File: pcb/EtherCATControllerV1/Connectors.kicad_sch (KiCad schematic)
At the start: 16 parts, among them J1 Conn_01x04, J2 Conn_01x05_Socket, J3 Conn_01x04_Socket, T1 H1102NLT

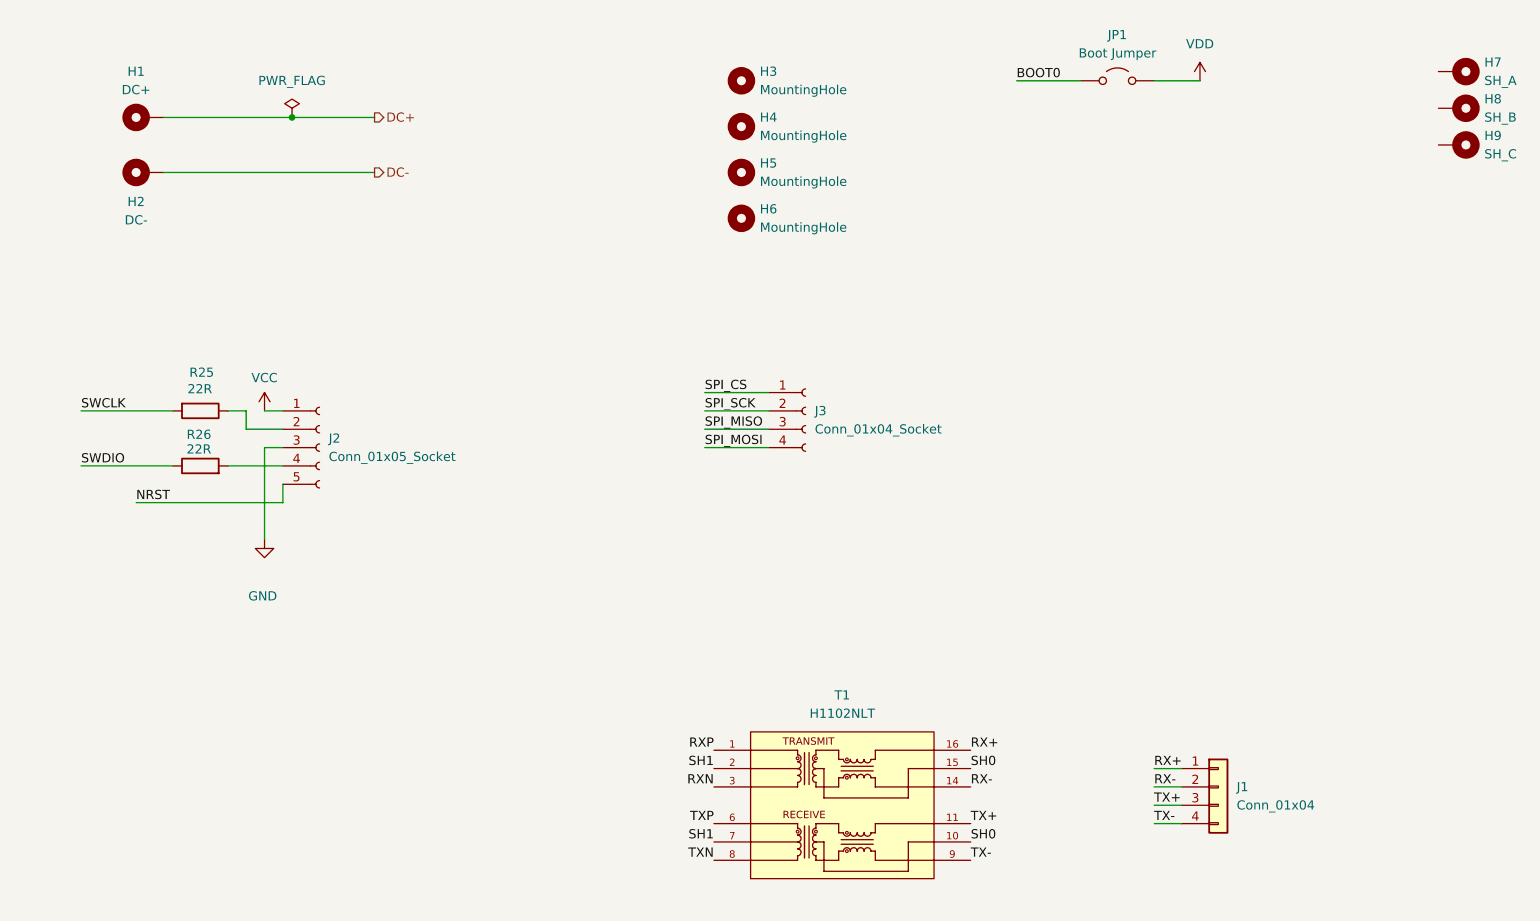
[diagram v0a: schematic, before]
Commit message: Initial design without Ethernet connectors
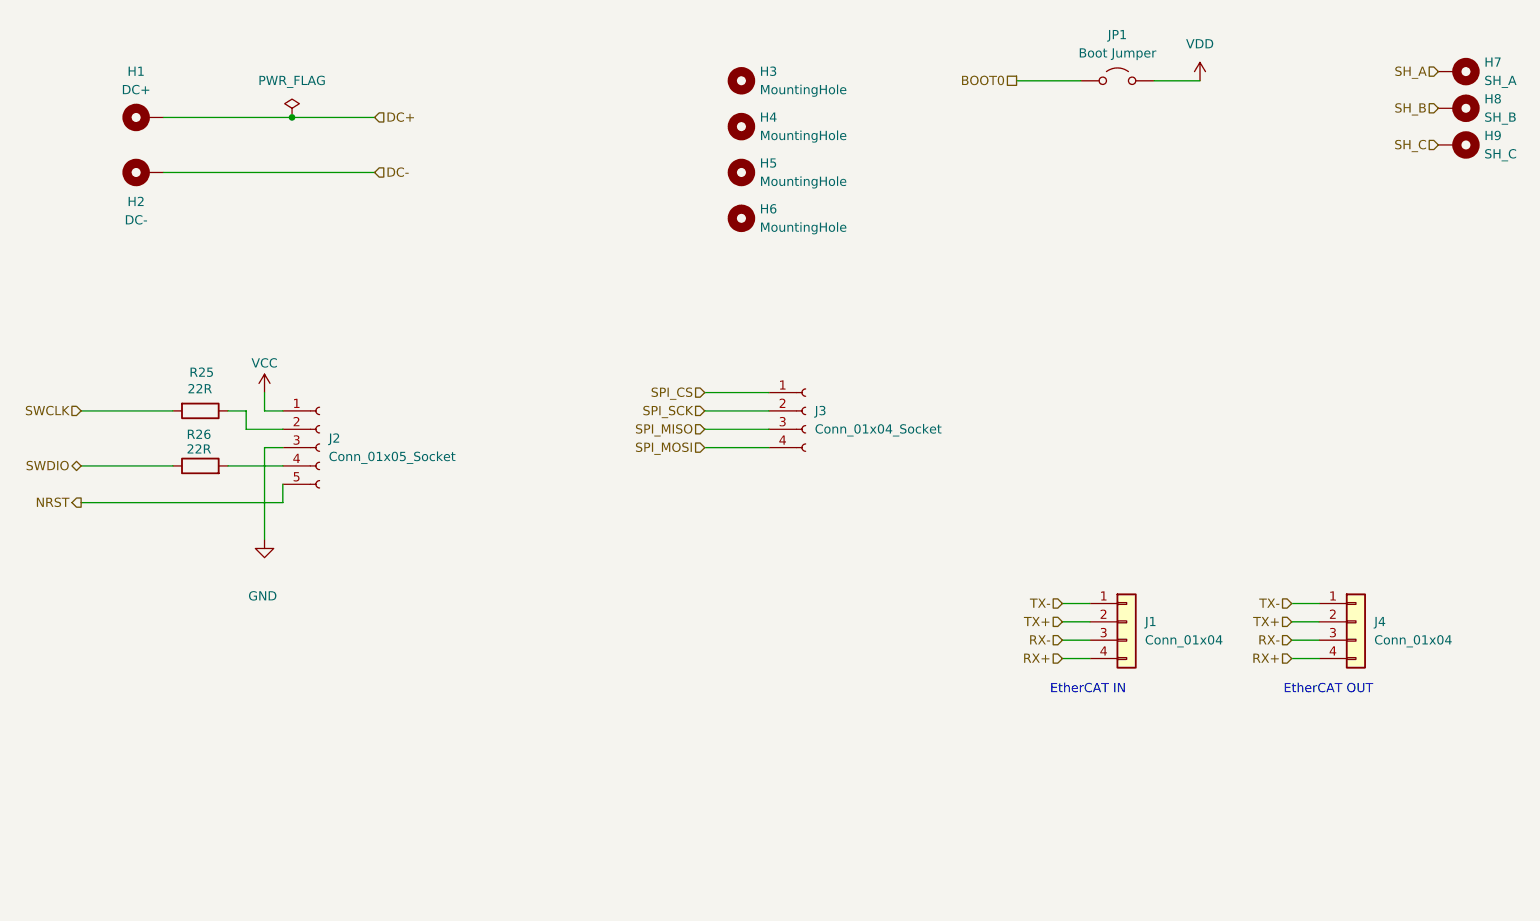
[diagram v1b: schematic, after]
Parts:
- removed T1: H1102NLT, Ethernet:XFMR_H1102NLT, symbol H1102NLT:H1102NLT
- added J4: Conn_01x04, Connector_Molex:Molex_PicoBlade_53048-0410_1x04_P1.25mm_Horizontal, symbol Connector_Generic:Conn_01x04
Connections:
- net RX+: now also J1.4 (Pin_4), J4.4 (Pin_4); no longer J1.1 (Pin_1)
- net RX-: now also J1.3 (Pin_3), J4.3 (Pin_3); no longer J1.2 (Pin_2)
- net TX+: now also J1.2 (Pin_2), J4.2 (Pin_2); no longer J1.3 (Pin_3)
- net TX-: now also J1.1 (Pin_1), J4.1 (Pin_1); no longer J1.4 (Pin_4)
- net SH_A: now reaches H7.1
- net SH_B: now reaches H8.1
- net SH_C: now reaches H9.1
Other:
- note added: "EtherCAT IN"
- note added: "EtherCAT OUT"
- moved on the sheet: J1

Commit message: Added IO Board project
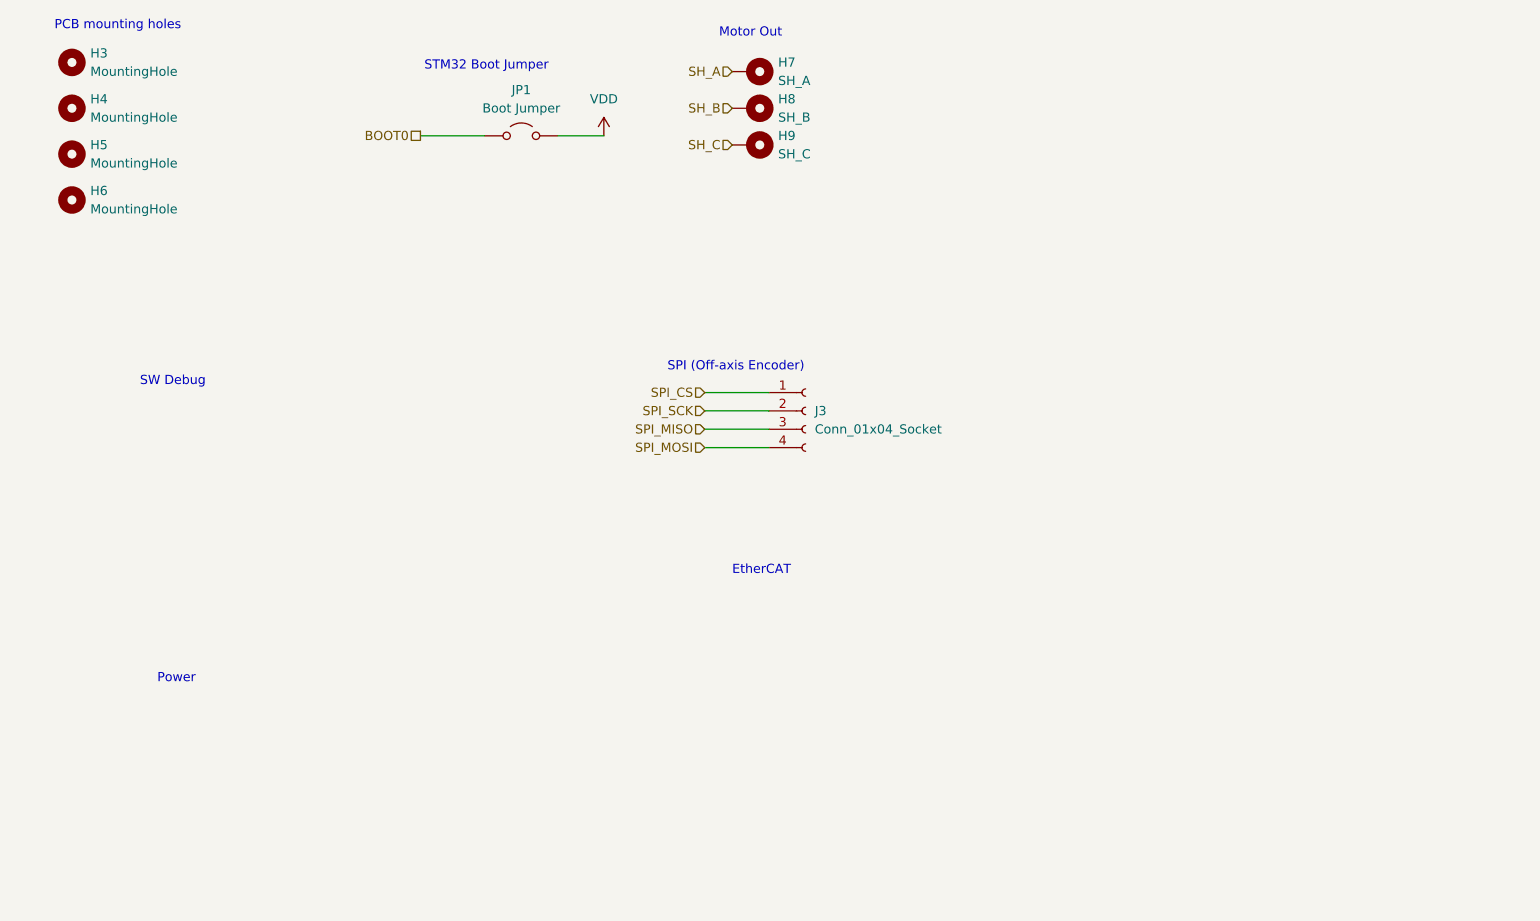
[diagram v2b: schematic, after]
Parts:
- removed H1: DC+, symbol Mechanical:MountingHole_Pad
- removed H2: DC-, symbol Mechanical:MountingHole_Pad
- removed J1, J4: Conn_01x04, Connector_Molex:Molex_PicoBlade_53048-0410_1x04_P1.25mm_Horizontal, symbol Connector_Generic:Conn_01x04
- removed J2: Conn_01x05_Socket, Hole-Mounts:Five-Hole, symbol Connector:Conn_01x05_Socket
- removed R25, R26: 22R, Resistor_SMD:R_0603_1608Metric, symbol Device:R
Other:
- note added: "EtherCAT"
- note added: "Motor Out"
- note added: "PCB mounting holes"
- note added: "Power"
- note added: "SPI (Off-axis Encoder)"
- note added: "STM32 Boot Jumper"
- note added: "SW Debug"
- note removed: "EtherCAT IN"
- note removed: "EtherCAT OUT"
- moved on the sheet: H3, H4, H5, H6, H7, H8, H9, JP1

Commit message: schematic finished, need to set proper ERCs
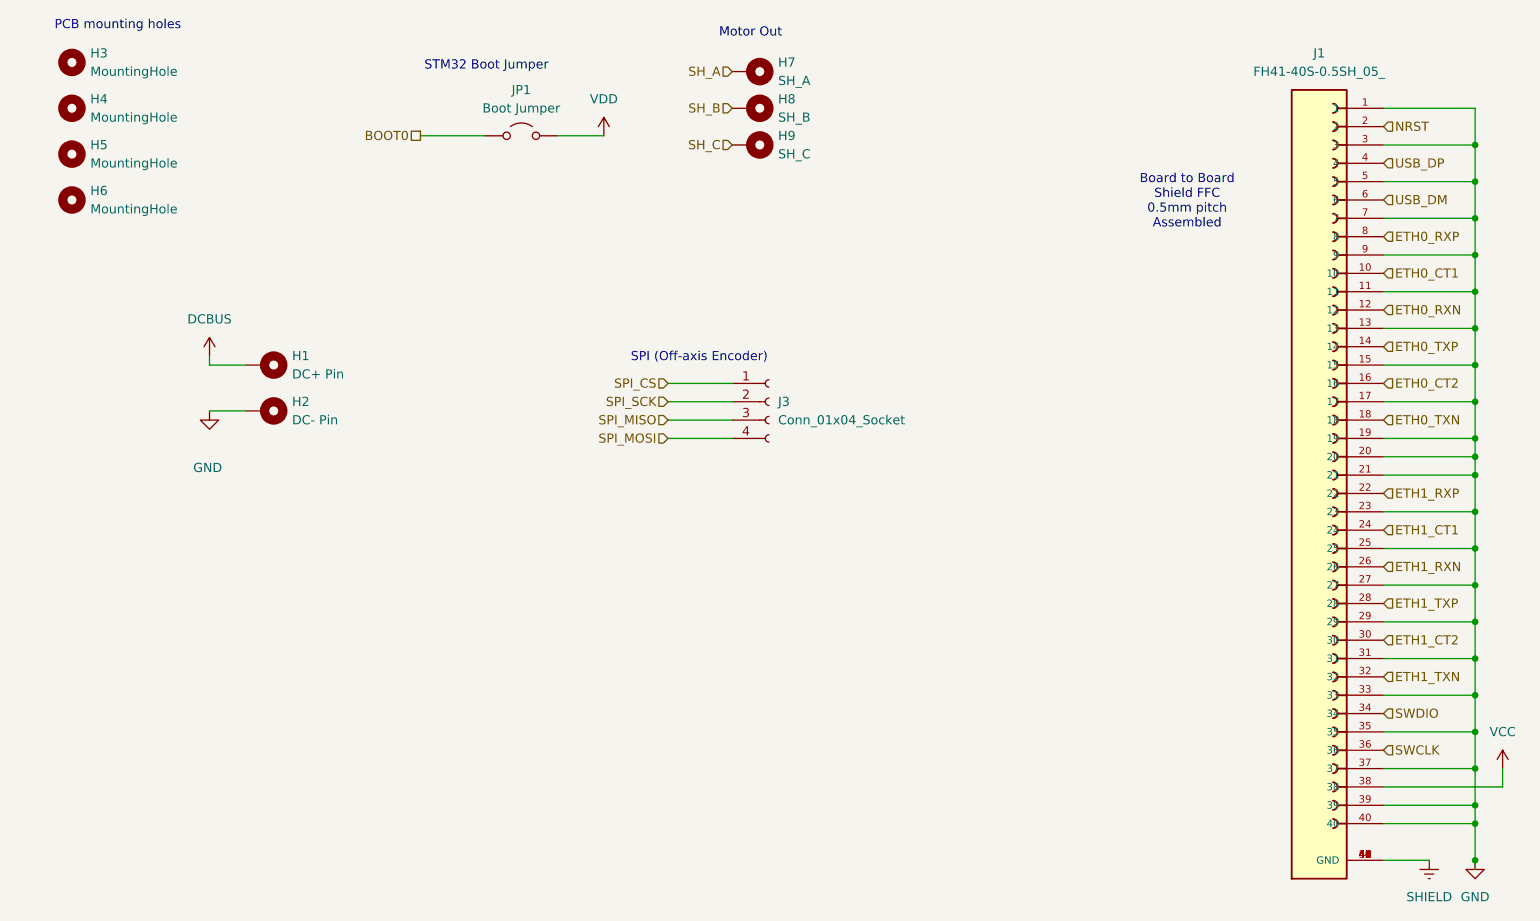
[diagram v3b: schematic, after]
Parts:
- added H1: DC+ Pin, symbol Mechanical:MountingHole_Pad
- added H2: DC- Pin, symbol Mechanical:MountingHole_Pad
- added J1: FH41-40S-0.5SH_05_, FH41-40S-0.5SH_05_:HRS_FH41-40S-0.5SH_05_, symbol FH41-40S-0.5SH_05_:FH41-40S-0.5SH_05_
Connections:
- new net DCBUS: H1.1
- new net ETH0_CT1: J1.10
- new net ETH0_CT2: J1.16
- new net ETH0_RXN: J1.12
- new net ETH0_RXP: J1.8
- new net ETH0_TXN: J1.18
- new net ETH0_TXP: J1.14
- new net ETH1_CT1: J1.24
- new net ETH1_CT2: J1.30
- new net ETH1_RXN: J1.26
- new net ETH1_RXP: J1.22
- new net ETH1_TXN: J1.32
- new net ETH1_TXP: J1.28
- new net GND: H2.1, J1.1, J1.11, J1.13, J1.15, J1.17, J1.19, J1.20, J1.21, J1.23, J1.25, J1.27, J1.29, J1.3, J1.31, J1.33, J1.35, J1.37, J1.39, J1.40, J1.5, J1.7, J1.9
- new net NRST: J1.2
- new net SHIELD: J1.41 (GND), J1.42 (GND), J1.43 (GND), J1.44 (GND), J1.45 (GND), J1.46 (GND), J1.47 (GND), J1.48 (GND), J1.49 (GND), J1.50 (GND)
- new net SWCLK: J1.36
- new net SWDIO: J1.34
- new net USB_DM: J1.6
- new net USB_DP: J1.4
- new net VCC: J1.38
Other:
- note added: "Board to Board Shield FFC 0.5mm pitch Assembled"
- note removed: "EtherCAT"
- note removed: "Power"
- note removed: "SW Debug"
- moved on the sheet: J3

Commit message: fix all ERCs
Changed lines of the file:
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@@
+	)
+	(junction
+		(at 217.17 139.7)
+		(diameter 0)
+		(color 0 0 0 0)
 	)
 	(junction
@@
 	(wire
 		(pts
+			(xy 217.17 139.7) (xy 220.98 139.7)
+		)
+		(stroke
+			(width 0)
+			(type default)
+		)
+	)
+	(wire
+		(pts
 			(xy 52.07 77.47) (xy 57.15 77.47)
 		)
@@
 	(wire
 		(pts
-			(xy 214.63 139.7) (xy 220.98 139.7)
+			(xy 214.63 139.7) (xy 217.17 139.7)
 		)
 		(stroke
@@
 					(unit 1)
 				)
+			)
+		)
+	)
+	(symbol
+		(lib_id "power:PWR_FLAG")
+		(at 217.17 139.7 0)
+		(unit 1)
+		(exclude_from_sim no)
+		(in_bom yes)
+		(on_board yes)
+		(dnp no)
+		(property "Reference" "#FLG010"
+			(at 217.17 137.795 0)
+			(effects
+				(font
+					(size 1.27 1.27)
+				)
+				(hide yes)
+			)
+		)
+		(property "Value" "PWR_FLAG"
+			(at 217.17 136.144 0)
+			(effects
+				(font
+					(size 1.27 1.27)
+				)
+			)
+		)
+		(property "Footprint" ""
+			(at 217.17 139.7 0)
+			(effects
+				(font
+					(size 1.27 1.27)
+				)
+				(hide yes)
+			)
+		)
+		(property "Datasheet" "~"
+			(at 217.17 139.7 0)
+			(effects
+				(font
+					(size 1.27 1.27)
+				)
+				(hide yes)
+			)
+		)
+		(property "Description" "Special symbol for telling ERC where power comes from"
+			(at 217.17 139.7 0)
+			(effects
+				(font
+					(size 1.27 1.27)
+				)
+				(hide yes)
+			)
+		)
+		(pin "1"
+		)
+		(instances
+			(project ""
+				(path "/4c927f80-855d-490a-80b2-e5c55283621a/6b6e615f-099d-4b57-8a21-048f9b8db3e5"
+					(reference "#FLG010")
+					(unit 1)
+				)
